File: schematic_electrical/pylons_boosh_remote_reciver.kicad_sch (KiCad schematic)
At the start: 0 parts

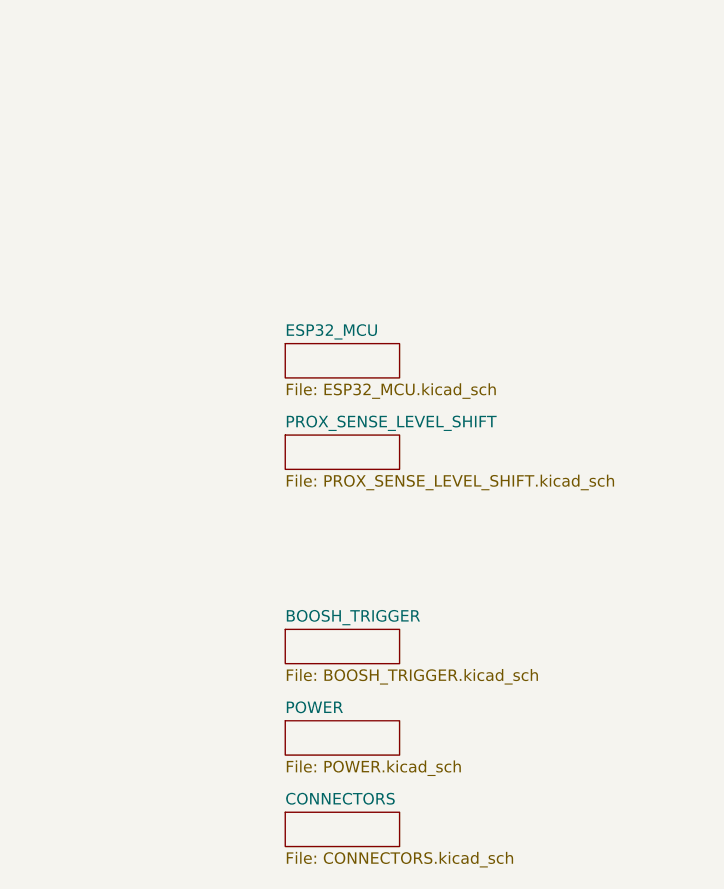
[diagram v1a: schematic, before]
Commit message: Schematic for fabrication. New symbols
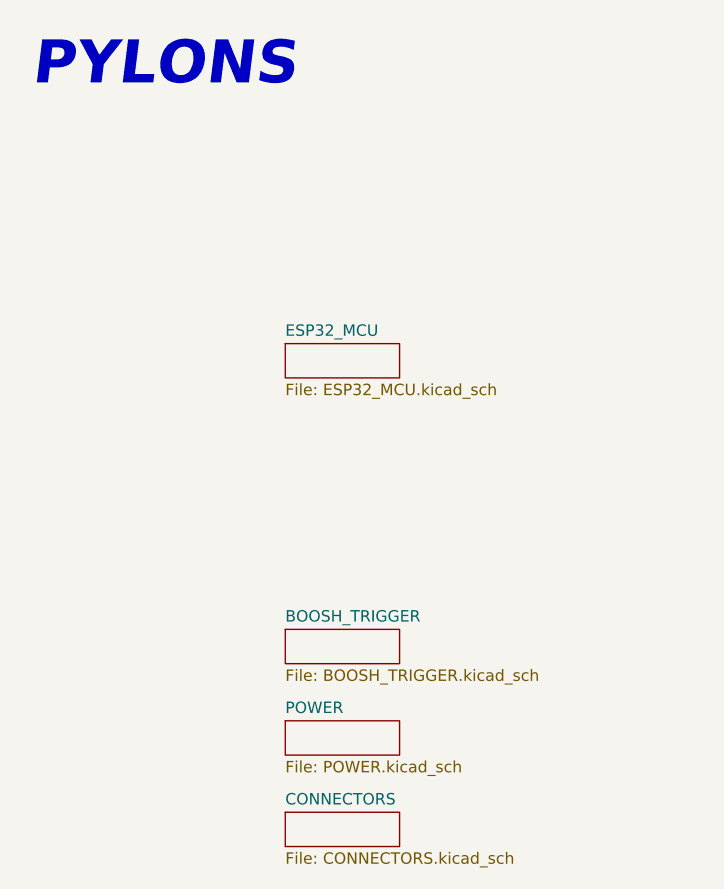
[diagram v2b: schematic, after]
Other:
- removed sheet PROX_SENSE_LEVEL_SHIFT
- note added: "PYLONS"
- title: BOOSH REMOTE RECEIVER -> PYLONS BOOSH REMOTE RECEIVER
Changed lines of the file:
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@@
 	(paper "A4")
 	(title_block
-		(title "BOOSH REMOTE RECEIVER")
+		(title "PYLONS BOOSH REMOTE RECEIVER")
 		(date "2026-03-10")
 		(company "MSW")
+	)
+	(text "PYLONS"
+		(exclude_from_sim no)
+		(at 30.988 19.812 0)
+		(effects
+			(font
+				(size 4.7752 4.7752)
+				(thickness 0.955)
+				(bold yes)
+				(italic yes)
+				(color 255 153 0 1)
+			)
+		)
 	)
 	(sheet
@@
 				)
 			)
-		)
-	)
-	(sheet
-		(at 44.45 60.96)
-		(size 12.7 3.81)
-		(fields_autoplaced yes)
-		(stroke
-			(width 0.1524)
-			(type solid)
-		)
-		(fill
-			(color 0 0 0 0.0000)
-		)
-		(property "Sheetname" "PROX_SENSE_LEVEL_SHIFT"
-			(at 44.45 60.2484 0)
-			(effects
-				(font
-					(size 1.27 1.27)
-				)
-				(justify left bottom)
-			)
-		)
-		(property "Sheetfile" "PROX_SENSE_LEVEL_SHIFT.kicad_sch"
-			(at 44.45 65.3546 0)
-			(effects
-				(font
-					(size 1.27 1.27)
-				)
-				(justify left top)
-			)
-		)
-		(instances
-			(project "pylons_boosh_remote_reciver"
-				(path "/f3653ac0-a28a-4ee8-bcf5-236139001455"
-					(page "3")
-				)
-			)
